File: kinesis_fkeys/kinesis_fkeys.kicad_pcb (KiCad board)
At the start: 2 copper layers, 132.6 x 61 mm, 40 parts, among them J1 RIGHT_13_TOP, J2 LEFT_13_TOP, J3 Conn_01x08, J5 Conn_01x08

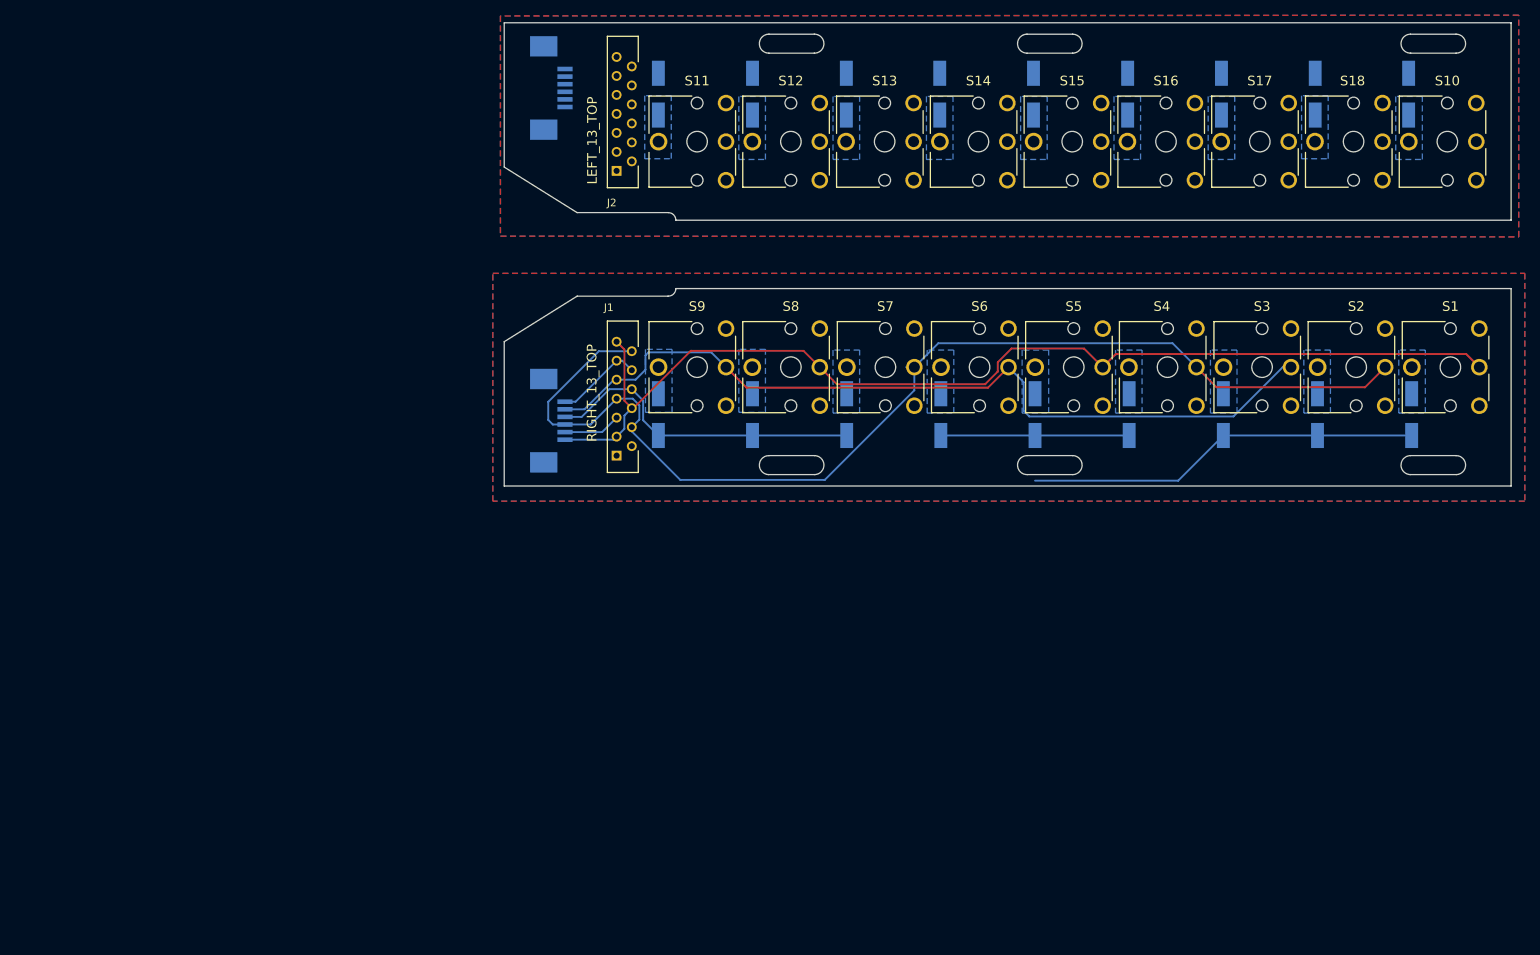
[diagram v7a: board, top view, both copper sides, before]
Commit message: created layout - needs to be modified a bit
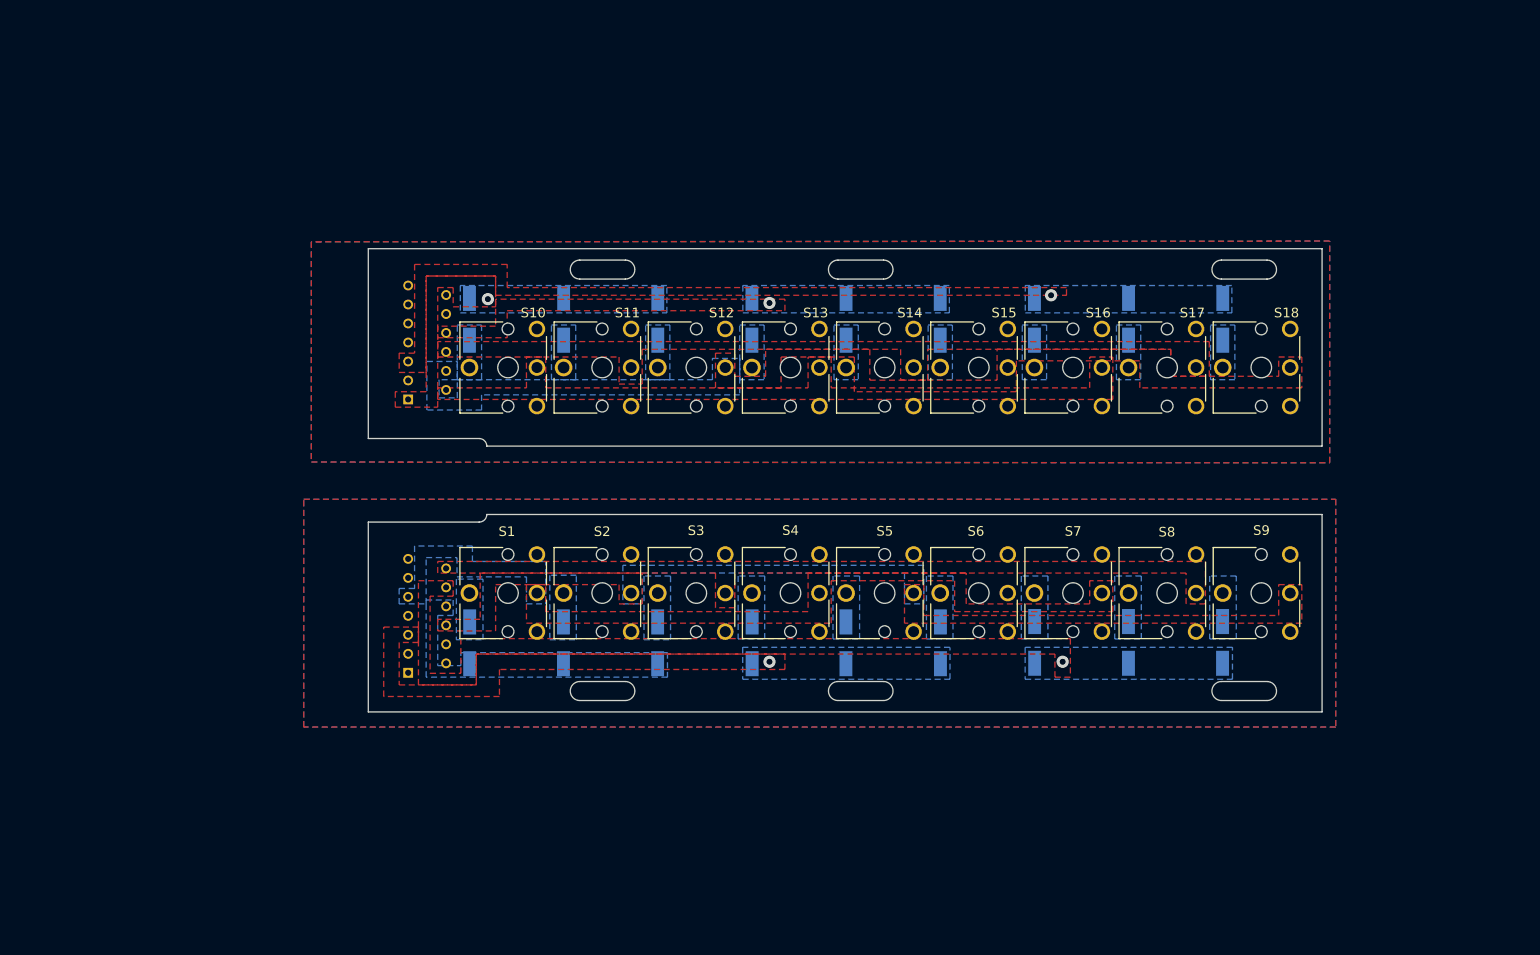
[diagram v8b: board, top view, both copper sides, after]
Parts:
- removed J2: LEFT_13_TOP, dodo_conn:Molex-39-53-2135
- removed J5: Conn_01x08, dodo_conn:84953-6
- J1: footprint dodo_conn:Molex-39-53-2135 -> dodo_conn:Molex-39-53-2134; moved to B.Cu
- J3: value Conn_01x08 -> LEFT_13_TOP; footprint dodo_conn:84953-6 -> dodo_conn:Molex-39-53-2134
- moved S1 127.6 mm to (116.4, 103.6)
- moved S10 127.2 mm to (116.4, 73.9)
- moved D1 103.7 mm to (132.3, 115.2), turned to 90 degrees
- moved S2 103.7 mm to (128.8, 103.6)
- moved D4 91.9 mm to (107.5, 115.2), turned to 90 degrees
- moved D2 80.3 mm to (144.7, 115.2), turned to 90 degrees
- moved S3 80.2 mm to (141.2, 103.6)
- moved D9 80.1 mm to (206.7, 115.2), turned to 90 degrees
- moved S9 80.0 mm to (215.6, 103.6)
- moved D5 69.0 mm to (119.9, 115.2), turned to 90 degrees
- moved D13 68.7 mm to (107.5, 72.6), turned to 90 degrees
- moved D3 58.1 mm to (157.1, 115.2), turned to 90 degrees
- moved D8 57.9 mm to (194.3, 115.2), turned to 90 degrees
- moved S4 57.9 mm to (153.6, 103.6)
- moved S8 57.8 mm to (203.2, 103.6)
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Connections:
- D1 pad 1: Net-(D1-K) -> /right_fkeys/COL_3
- D1 pad 2: /right_fkeys/COL_5 -> Net-(D1-A)
- D10 pad 1: /left_fkeys/COL_1 -> Net-(D10-K)
- D10 pad 2: Net-(D10-A) -> /left_fkeys/COL_0
- D11 pad 1: /left_fkeys/COL_2 -> Net-(D11-K)
- D11 pad 2: Net-(D11-A) -> /left_fkeys/COL_1
- D12 pad 1: /left_fkeys/COL_2 -> Net-(D12-K)
- D12 pad 2: Net-(D12-A) -> /left_fkeys/COL_1
- D13 pad 1: /left_fkeys/COL_1 -> Net-(D13-K)
- D13 pad 2: Net-(D13-A) -> /left_fkeys/COL_0
- D14 pad 1: /left_fkeys/COL_2 -> Net-(D14-K)
- D14 pad 2: Net-(D14-A) -> /left_fkeys/COL_0
- D15 pad 1: /left_fkeys/COL_1 -> Net-(D15-K)
- D15 pad 2: Net-(D15-A) -> /left_fkeys/COL_1
- D16 pad 1: /left_fkeys/COL_0 -> Net-(D16-K)
- D16 pad 2: Net-(D16-A) -> /left_fkeys/COL_2
- D17 pad 1: /left_fkeys/COL_0 -> Net-(D17-K)
- D17 pad 2: Net-(D17-A) -> /left_fkeys/COL_2
- D18 pad 1: /left_fkeys/COL_0 -> Net-(D18-K)
- D18 pad 2: Net-(D18-A) -> /left_fkeys/COL_2
- D2 pad 1: Net-(D2-K) -> /right_fkeys/COL_4
- D2 pad 2: /right_fkeys/COL_5 -> Net-(D2-A)
- D3 pad 1: Net-(D3-K) -> /right_fkeys/COL_4
- D3 pad 2: /right_fkeys/COL_5 -> Net-(D3-A)
- D4 pad 1: Net-(D4-K) -> /right_fkeys/COL_3
- D4 pad 2: /right_fkeys/COL_4 -> Net-(D4-A)
- D5 pad 1: Net-(D5-K) -> /right_fkeys/COL_3
- D5 pad 2: /right_fkeys/COL_4 -> Net-(D5-A)
- D6 pad 1: Net-(D6-K) -> /right_fkeys/COL_4
- D6 pad 2: /right_fkeys/COL_4 -> Net-(D6-A)
- D7 pad 1: Net-(D7-K) -> /right_fkeys/COL_5
- D7 pad 2: /right_fkeys/COL_3 -> Net-(D7-A)
- D8 pad 1: Net-(D8-K) -> /right_fkeys/COL_5
- D8 pad 2: /right_fkeys/COL_3 -> Net-(D8-A)
- D9 pad 1: Net-(D9-K) -> /right_fkeys/COL_5
- D9 pad 2: /right_fkeys/COL_3 -> Net-(D9-A)
- J1 pad 11: /right_fkeys/COL_5 -> /right_fkeys/COL_5_
- J1 pad 13: /right_fkeys/ROW_F1 -> /right_fkeys/ROW_F1__
- J1 pad 3: /right_fkeys/ROW_F1 -> /right_fkeys/ROW_F1_
- J1 pad 4: /right_fkeys/ROW_F2 -> /right_fkeys/ROW_F2__
- J1 pad 7: /right_fkeys/ROW_F2 -> /right_fkeys/ROW_F2_
- J3 pad 1: /right_fkeys/ROW_F1 -> /left_fkeys/COL_0
- J3 pad 2: /right_fkeys/COL_4 -> /left_fkeys/ROW_ESC
- J3 pad 3: /right_fkeys/ROW_F2 -> /left_fkeys/__ROW_F1
- J3 pad 4: /right_fkeys/COL_3 -> /left_fkeys/ROW_F2
- J3 pad 5: /right_fkeys/ROW_ESC -> /left_fkeys/COL_2
- J3 pad 6: /right_fkeys/COL_5 -> /left_fkeys/ROW_F1
- J3 pad 7: GND_R -> /left_fkeys/ROW_F2__
- J3 pad 8: GND_R -> /left_fkeys/COL_1
- S1 pad 2: /right_fkeys/ROW_F1 -> /right_fkeys/ROW_ESC
- S1 pad 4: Net-(D1-K) -> Net-(D4-A)
- S10 pad 4: Net-(D18-A) -> Net-(D13-K)
- S11 pad 2: /left_fkeys/ROW_F2 -> /left_fkeys/ROW_F1
- S11 pad 4: Net-(D14-A) -> Net-(D14-K)
- S12 pad 1: GND -> GND_L
- S12 pad 2: /left_fkeys/ROW_F1 -> /left_fkeys/ROW_F2
- S12 pad 3: GND -> GND_L
- S12 pad 4: Net-(D11-A) -> Net-(D10-K)
- S13 pad 4: Net-(D12-A) -> Net-(D11-K)
- S14 pad 2: /left_fkeys/ROW_F2 -> /left_fkeys/ROW_F1
- S14 pad 4: Net-(D13-A) -> Net-(D12-K)
- S15 pad 2: /left_fkeys/ROW_F1 -> /left_fkeys/ROW_F2
- S15 pad 4: Net-(D10-A) -> Net-(D15-K)
- S16 pad 4: Net-(D15-A) -> Net-(D16-K)
- S17 pad 2: /left_fkeys/ROW_F2 -> /left_fkeys/ROW_F1
- S17 pad 4: Net-(D16-A) -> Net-(D17-K)
- S18 pad 2: /left_fkeys/ROW_F1 -> /left_fkeys/ROW_F2
- S18 pad 4: Net-(D17-A) -> Net-(D18-K)
- S2 pad 2: /right_fkeys/ROW_F2 -> /right_fkeys/ROW_F1
- S2 pad 4: Net-(D2-K) -> Net-(D5-A)
- S3 pad 2: /right_fkeys/ROW_ESC -> /right_fkeys/ROW_F2
- S3 pad 4: Net-(D3-K) -> Net-(D1-A)
- S4 pad 2: /right_fkeys/ROW_F2 -> /right_fkeys/ROW_ESC
- S4 pad 4: Net-(D4-K) -> Net-(D2-A)
- S5 pad 4: Net-(D5-K) -> Net-(D3-A)
- S6 pad 2: /right_fkeys/ROW_ESC -> /right_fkeys/ROW_F2
- S6 pad 4: Net-(D6-K) -> Net-(D6-A)
- S7 pad 2: /right_fkeys/ROW_F2 -> /right_fkeys/ROW_ESC
- S7 pad 4: Net-(D7-K) -> Net-(D7-A)
- S8 pad 2: /right_fkeys/ROW_F1 -> /right_fkeys/ROW_F2
- S8 pad 4: Net-(D8-K) -> Net-(D8-A)
- S9 pad 2: /right_fkeys/ROW_ESC -> /right_fkeys/ROW_F1
- S9 pad 4: Net-(D9-K) -> Net-(D9-A)
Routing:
- net /right_fkeys/ROW_F2: track 149.7 -> 0.00 mm
- net /right_fkeys/ROW_F1: track 142.8 -> 0.00 mm
- net /right_fkeys/ROW_ESC: track 110.5 -> 0.00 mm
- net /right_fkeys/COL_5: track 63.6 -> 0.00 mm, vias 0 -> 1
- net /right_fkeys/COL_3: track 42.7 -> 0.00 mm
- net /right_fkeys/COL_4: track 32.4 -> 0.00 mm, vias 0 -> 1
- net /left_fkeys/COL_2: vias 0 -> 1
- net /left_fkeys/COL_1: vias 0 -> 1
- net /left_fkeys/COL_0: vias 0 -> 1
- added copper zone on B.Cu, net /left_fkeys/COL_0
- added copper zone on F.Cu, net /left_fkeys/COL_0
- added copper zone on B.Cu, net /left_fkeys/COL_1
- added copper zone on F.Cu, net /left_fkeys/COL_1
- added copper zone on B.Cu, net /left_fkeys/COL_2
- added copper zone on F.Cu, net /left_fkeys/COL_2
- added copper zone on F.Cu, net /left_fkeys/ROW_ESC
- added copper zone on F.Cu, net /left_fkeys/ROW_F1
- added copper zone on B.Cu, net /left_fkeys/ROW_F2
- added copper zone on F.Cu, net /left_fkeys/ROW_F2
- added copper zone on B.Cu, net /right_fkeys/COL_3
- added copper zone on B.Cu, net /right_fkeys/COL_4
- added copper zone on F.Cu, net /right_fkeys/COL_4
- added copper zone on B.Cu, net /right_fkeys/COL_5
- added copper zone on F.Cu, net /right_fkeys/COL_5
- added copper zone on B.Cu, net /right_fkeys/ROW_ESC
- added copper zone on F.Cu, net /right_fkeys/ROW_ESC
- added copper zone on F.Cu, net /right_fkeys/ROW_F1
- added copper zone on B.Cu, net /right_fkeys/ROW_F2
- added copper zone on F.Cu, net /right_fkeys/ROW_F2
- added copper zone on B.Cu, net GND_L
- added copper zone on F.Cu, net GND_L
- added copper zone on B.Cu, net Net-(D1-A)
- added copper zone on B.Cu, net Net-(D10-K)
- added copper zone on B.Cu, net Net-(D11-K)
- added copper zone on B.Cu, net Net-(D12-K)
- added copper zone on B.Cu, net Net-(D13-K)
- added copper zone on B.Cu, net Net-(D14-K)
- added copper zone on B.Cu, net Net-(D15-K)
- added copper zone on B.Cu, net Net-(D16-K)
- added copper zone on B.Cu, net Net-(D17-K)
- added copper zone on B.Cu, net Net-(D18-K)
- added copper zone on B.Cu, net Net-(D2-A)
- added copper zone on B.Cu, net Net-(D3-A)
- added copper zone on B.Cu, net Net-(D4-A)
- added copper zone on B.Cu, net Net-(D5-A)
- added copper zone on B.Cu, net Net-(D6-A)
- added copper zone on B.Cu, net Net-(D7-A)
- added copper zone on B.Cu, net Net-(D8-A)
- added copper zone on B.Cu, net Net-(D9-A)
- removed copper zone on B.Cu, net Net-(D1-K)
- removed copper zone on B.Cu, net Net-(D10-A)
- removed copper zone on B.Cu, net Net-(D11-A)
- removed copper zone on B.Cu, net Net-(D12-A)
- removed copper zone on B.Cu, net Net-(D13-A)
- removed copper zone on B.Cu, net Net-(D14-A)
- removed copper zone on B.Cu, net Net-(D15-A)
- removed copper zone on B.Cu, net Net-(D16-A)
- removed copper zone on B.Cu, net Net-(D17-A)
- removed copper zone on B.Cu, net Net-(D18-A)
- removed copper zone on B.Cu, net Net-(D2-K)
- removed copper zone on B.Cu, net Net-(D3-K)
- removed copper zone on B.Cu, net Net-(D4-K)
- removed copper zone on B.Cu, net Net-(D5-K)
- removed copper zone on B.Cu, net Net-(D6-K)
- removed copper zone on B.Cu, net Net-(D7-K)
- removed copper zone on B.Cu, net Net-(D8-K)
- removed copper zone on B.Cu, net Net-(D9-K)
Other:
- board size 132.6 x 61 mm -> 125.6 x 61 mm
